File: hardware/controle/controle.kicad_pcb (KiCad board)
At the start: 2 copper layers, 97 x 67.8 mm, 82 parts, among them J1 Barrel_Jack, J10 Conn_01x05_Pin, J11 PWM, J12 ADC, J2 Serial, J3 PWR, J4 DATA, J5 UART7, J6 TWI3, J7 SENS0375, J8 TWI4, J9 LED, Q1 DMG2307L, Q2 DMG2307L, Q3 BSS123, Q4 BSS123, U1 MCP2003B, U2 MCP7940N-xSN, U3 TPS54228, U4 ULN2003, U5 PIC18F05Q40, Y1 32.768Khz

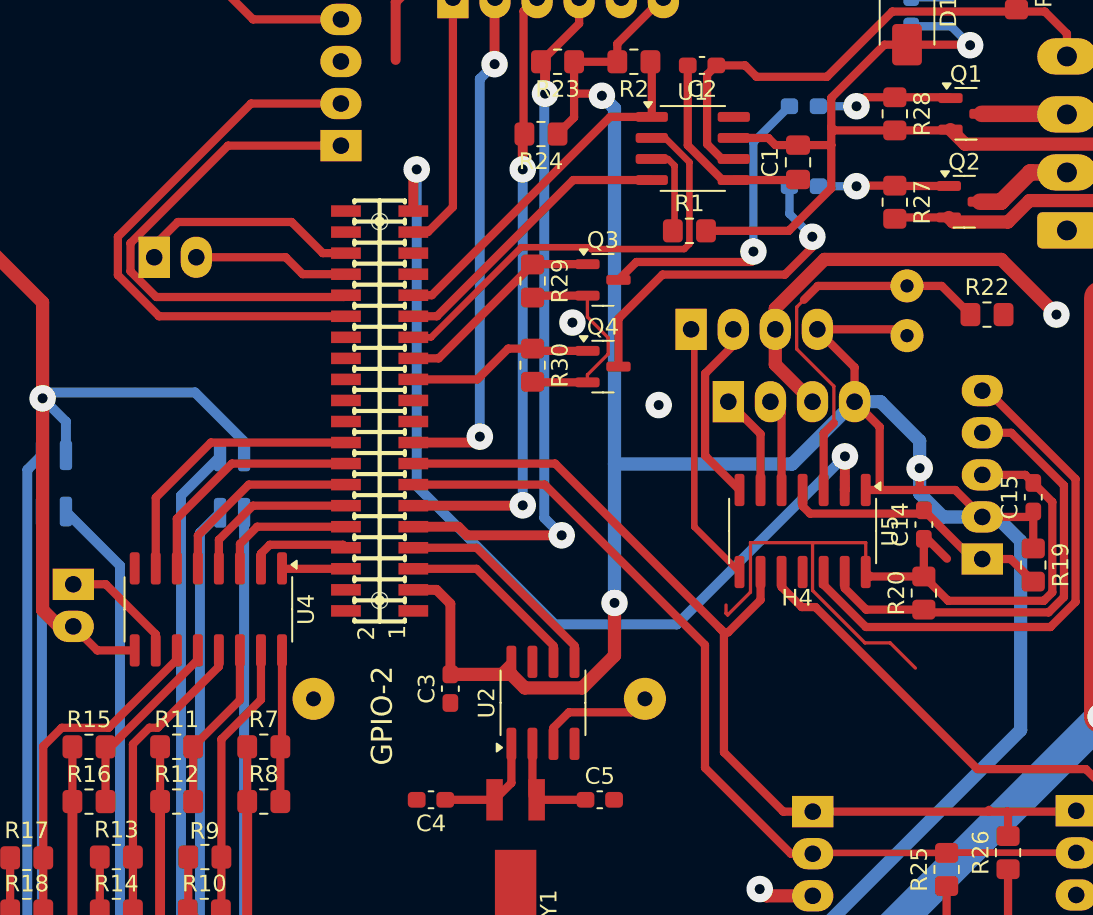
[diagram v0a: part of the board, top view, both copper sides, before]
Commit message: controle: update for DRC
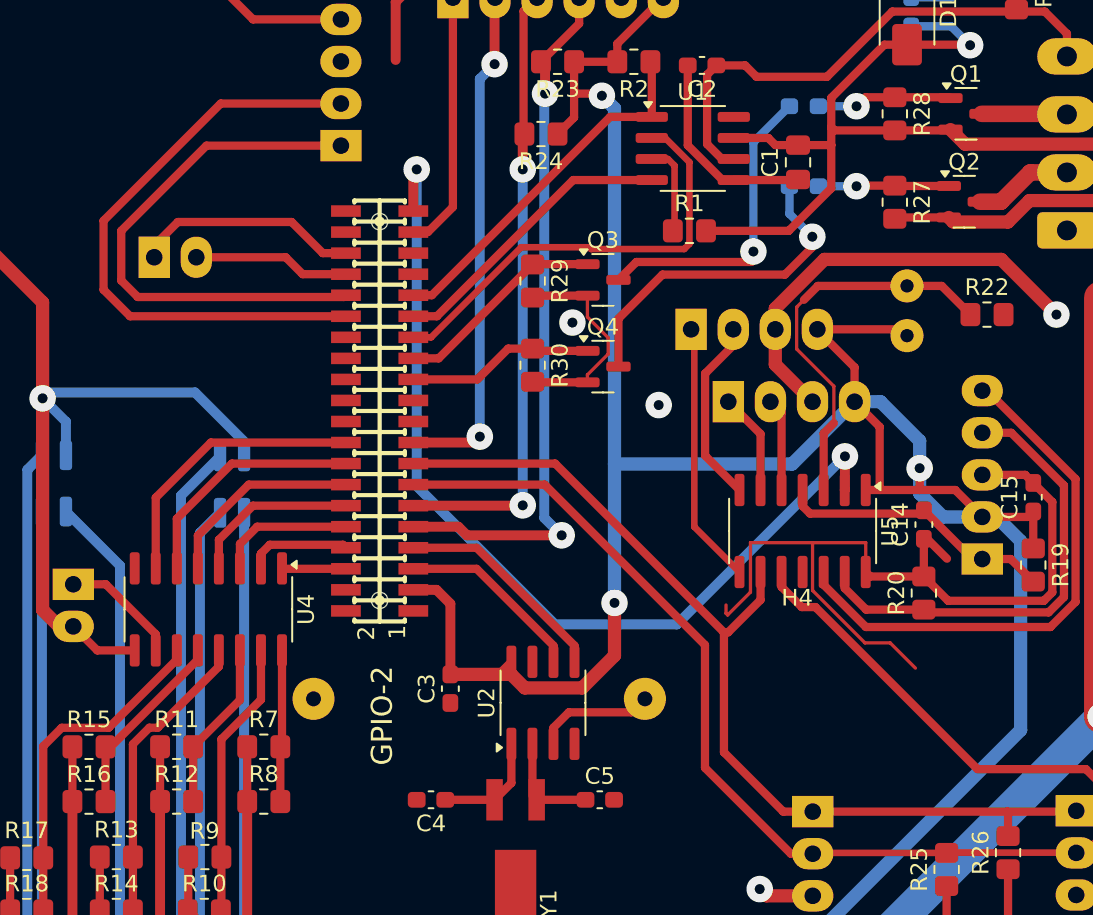
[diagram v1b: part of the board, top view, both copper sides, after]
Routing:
- net /PI21: track 33.9 -> 36.7 mm
- net /PI20: track 30.5 -> 32.4 mm
- net /PI18/UART2_TX: track 13.6 -> 12.9 mm
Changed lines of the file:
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@@
 	)
 	(segment
-		(start 72.0444 77.3076)
+		(start 64.745 90.145)
+		(end 63.1444 88.5444)
+		(width 0.5)
+		(layer "F.Cu")
+		(net 34)
+	)
+	(segment
+		(start 77.773 90.145)
+		(end 64.745 90.145)
+		(width 0.5)
+		(layer "F.Cu")
+		(net 34)
+	)
+	(segment
+		(start 70.2156 77.3076)
 		(end 77.47 77.3076)
 		(width 0.5)
@@
 	)
 	(segment
-		(start 64.008 85.344)
-		(end 72.0444 77.3076)
+		(start 63.1444 88.5444)
+		(end 63.1444 84.3788)
 		(width 0.5)
 		(layer "F.Cu")
@@
 	)
 	(segment
-		(start 77.773 90.145)
-		(end 66.493151 90.145)
-		(width 0.5)
-		(layer "F.Cu")
-		(net 34)
-	)
-	(segment
-		(start 64.008 87.659849)
-		(end 64.008 85.344)
-		(width 0.5)
-		(layer "F.Cu")
-		(net 34)
-	)
-	(segment
-		(start 66.493151 90.145)
-		(end 64.008 87.659849)
+		(start 63.1444 84.3788)
+		(end 70.2156 77.3076)
 		(width 0.5)
 		(layer "F.Cu")
@@
 	)
 	(segment
-		(start 70.655301 79.8476)
-		(end 77.47 79.8476)
-		(width 0.5)
-		(layer "F.Cu")
-		(net 46)
-	)
-	(segment
-		(start 64.77 85.732901)
-		(end 70.655301 79.8476)
-		(width 0.5)
-		(layer "F.Cu")
-		(net 46)
-	)
-	(segment
-		(start 64.77 87.431899)
-		(end 64.77 85.732901)
+		(start 65.208 88.9824)
+		(end 64.2112 87.9856)
 		(width 0.5)
 		(layer "F.Cu")
@@
 	)
 	(segment
-		(start 66.320501 88.9824)
-		(end 64.77 87.431899)
+		(start 64.2112 87.9856)
+		(end 64.2112 84.9884)
 		(width 0.5)
 		(layer "F.Cu")
@@
 	)
 	(segment
+		(start 69.352 79.8476)
+		(end 77.47 79.8476)
+		(width 0.5)
+		(layer "F.Cu")
+		(net 46)
+	)
+	(segment
+		(start 64.2112 84.9884)
+		(end 69.352 79.8476)
+		(width 0.5)
+		(layer "F.Cu")
+		(net 46)
+	)
+	(segment
 		(start 77.6656 88.9824)
-		(end 66.320501 88.9824)
+		(end 65.208 88.9824)
 		(width 0.5)
 		(layer "F.Cu")
@@
 	)
 	(segment
-		(start 66.2004 85.883)
-		(end 66.2004 86.5824)
-		(width 0.5)
-		(layer "F.Cu")
-		(net 54)
-	)
-	(segment
 		(start 76.37384 86.335)
 		(end 74.49384 84.455)
@@
 	)
 	(segment
-		(start 100.584 109.22)
-		(end 90.399 99.035)
+		(start 90.399 99.035)
+		(end 100.584 109.22)
 		(width 0.5)
 		(layer "F.Cu")
@@
 	)
 	(segment
-		(start 116.586 120.0404)
-		(end 116.586 119.929684)
-		(width 0.5)
-		(layer "F.Cu")
-		(net 56)
-	)
-	(segment
 		(start 102.7924 107.2656)
 		(end 100.838 109.22)
@@
 		(width 0.5)
 		(layer "F.Cu")
-		(net 56)
-	)
-	(segment
-		(start 100.33 108.966)
-		(end 100.584 109.22)
-		(width 0.5)
-		(layer "F.Cu")

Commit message: hardware/controle: adjust RGB leds resistors
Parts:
- R10, R16: value 330 -> 1k
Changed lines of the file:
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@@
 		(sheetname "LIN")
 		(sheetfile "lin.kicad_sch")
-		(attr smd)
+		(attr smd dnp)
 		(fp_line
 			(start -3.51 1.65)
@@
 			)
 		)
-		(property "Value" "330"
+		(property "Value" "1k"
 			(at 0 1.65 0)
 			(layer "F.Fab")
@@
 			)
 		)
-		(property "Value" "330"
+		(property "Value" "1k"
 			(at 0 1.65 0)
 			(layer "F.Fab")

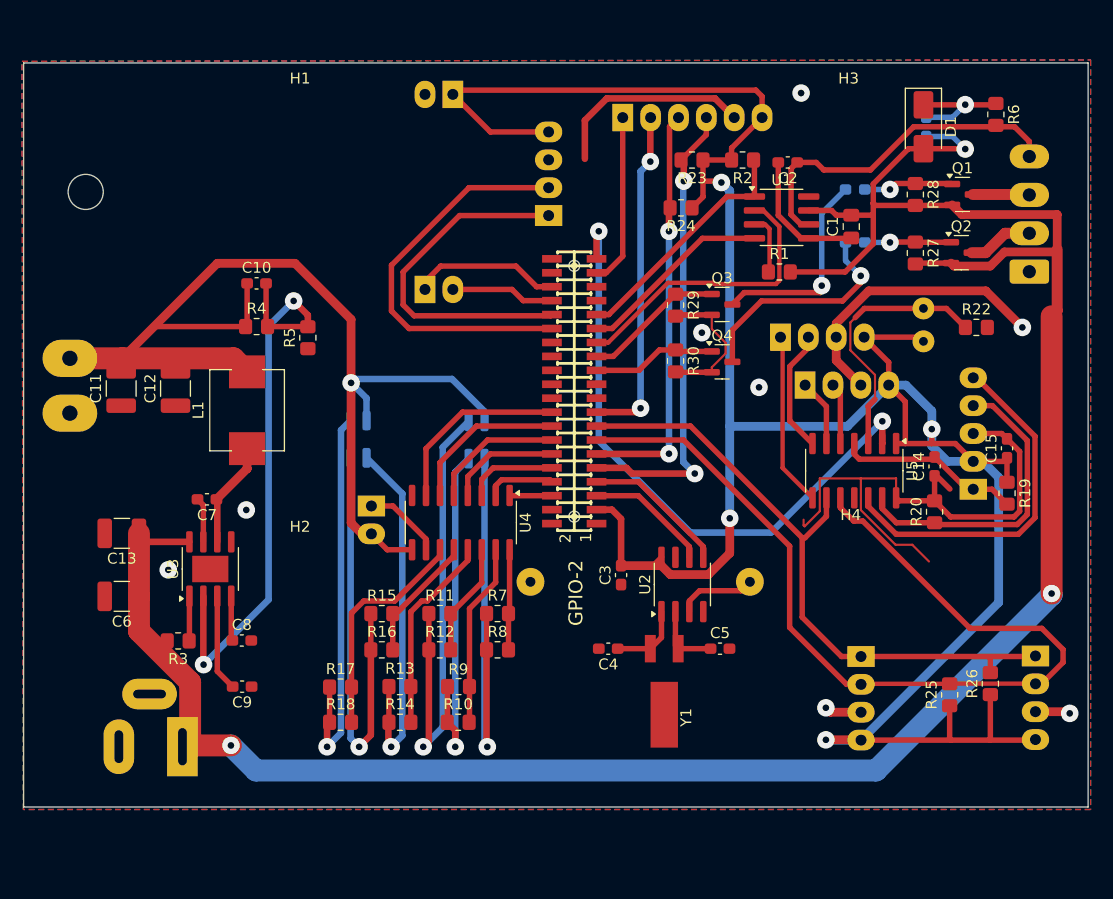
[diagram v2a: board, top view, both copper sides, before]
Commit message: hardware/controle: add fiducials (for OpenPnP)
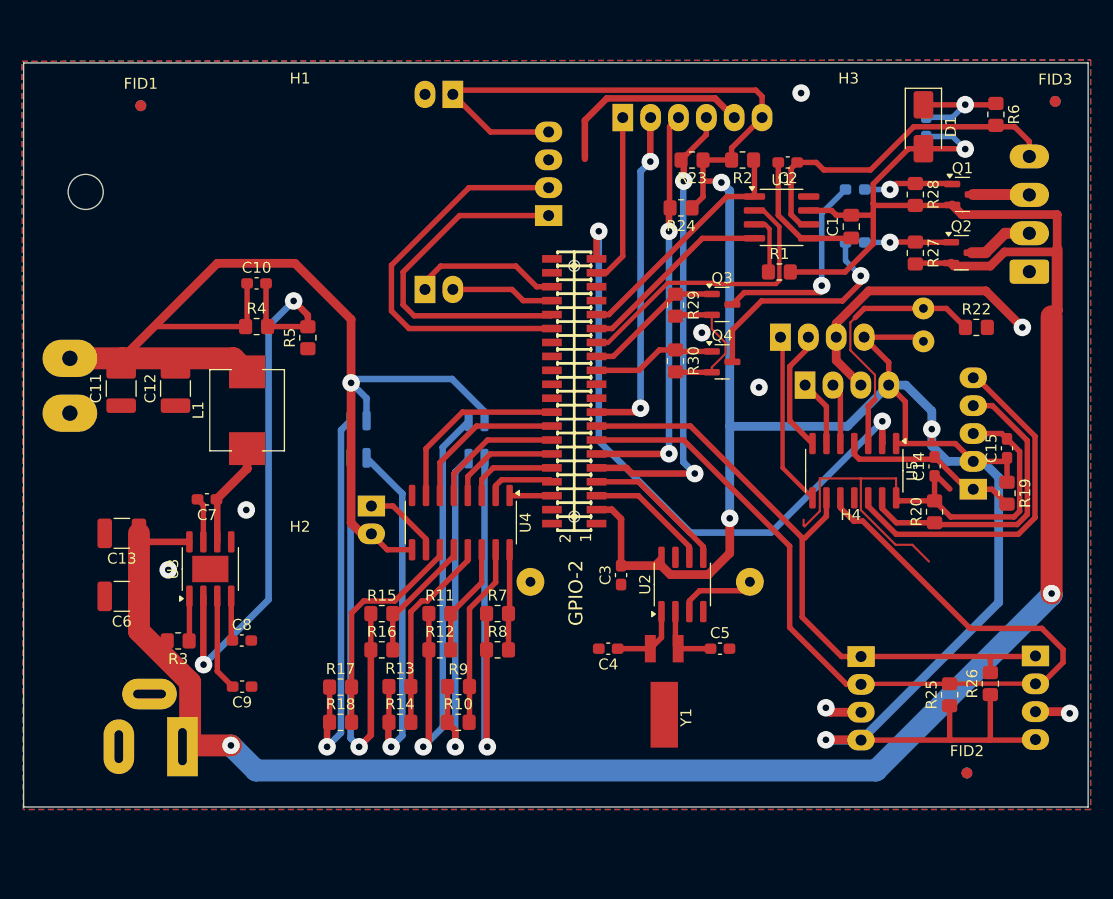
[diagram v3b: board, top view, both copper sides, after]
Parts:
- added FID1: Fiducial, Fiducial:Fiducial_1mm_Mask2mm, F.Cu at (40.3, 69.8)
- added FID2: Fiducial, Fiducial:Fiducial_1mm_Mask2mm, F.Cu at (115.6, 130.7)
- added FID3: Fiducial, Fiducial:Fiducial_1mm_Mask2mm, F.Cu at (123.6, 69.4)
- added FID4: Fiducial, Fiducial:Fiducial_1mm_Mask2mm, B.Cu at (40.3, 69.8)
- added FID5: Fiducial, Fiducial:Fiducial_1mm_Mask2mm, B.Cu at (115.6, 130.7)
- added FID6: Fiducial, Fiducial:Fiducial_1mm_Mask2mm, B.Cu at (123.6, 69.4)

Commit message: hardware/controle: re-route so that most connectors are on left and right sides, same as the lime2 board
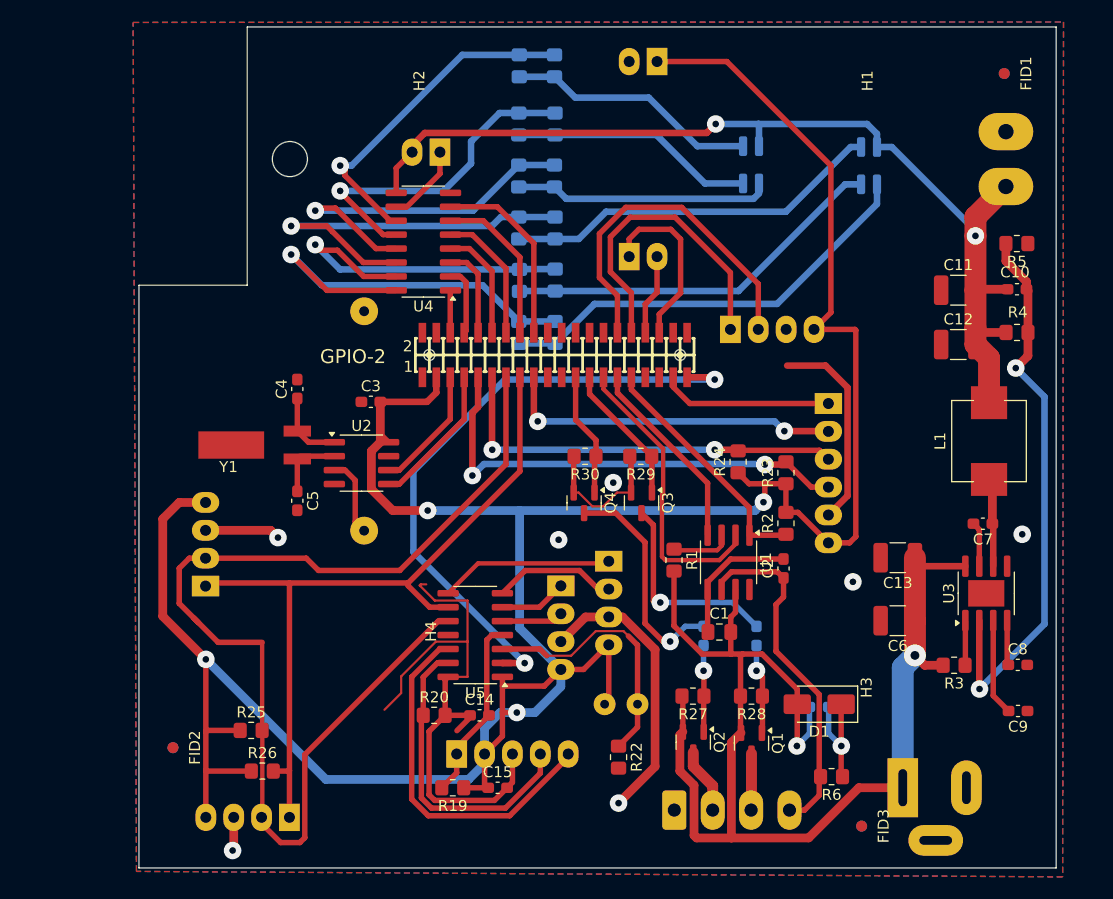
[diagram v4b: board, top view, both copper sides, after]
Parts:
- R10, R11, R12, R13, R14, R15, R16, R17, R18, R7, R8, R9: moved to B.Cu
- moved +5V1 87.8 mm to (119.2, 74.7), turned to -90 degrees
- moved FID1 78.8 mm to (119.0, 66.9), turned to -90 degrees
- moved FID4 78.8 mm to (119.0, 66.9), turned to 90 degrees
- moved C11 76.8 mm to (114.8, 86.7), turned to 0 degrees
- moved J7 75.9 mm to (46.2, 113.6), turned to 0 degrees
- moved FID2 72.4 mm to (43.2, 128.3), turned to -90 degrees
- moved FID5 72.4 mm to (43.2, 128.3), turned to 90 degrees
- moved C12 71.5 mm to (114.8, 91.6), turned to 0 degrees
- moved C13 70.8 mm to (109.3, 111.0)
- moved C6 70.8 mm to (109.3, 116.8)
- moved C8 70.8 mm to (120.2, 120.8)
- moved C7 70.8 mm to (117.1, 107.9)
- moved U3 70.8 mm to (117.4, 114.3)
- moved C9 70.8 mm to (120.3, 125.0)
- moved R3 70.8 mm to (114.4, 120.8)
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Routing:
- net +12V: track 212.8 -> 114.6 mm, vias 3 -> 2
- net +3V3: track 231.1 -> 262.1 mm
- net Net-(U4-O1): track 9.02 -> 37.5 mm, vias 0 -> 1
- net Net-(U4-O3): track 10.3 -> 35.4 mm, vias 0 -> 1
- net Net-(U4-O5): track 10.7 -> 30.0 mm, vias 0 -> 1
- net /PI2/TWI4_SCK: track 84.0 -> 102.3 mm
- net Net-(D3-GK): track 39.2 -> 22.3 mm, vias 1 -> 0
- net Net-(U4-O2): track 16.7 -> 31.4 mm, vias 0 -> 1
- net Net-(U4-O4): track 18.2 -> 32.5 mm, vias 0 -> 1
- net Net-(D3-BK): track 35.8 -> 23.0 mm, vias 1 -> 0
- net /power/+5VCPU: track 103.0 -> 91.7 mm, vias 1 -> 2
- net Net-(U4-O6): track 20.2 -> 30.6 mm, vias 0 -> 1
- net Net-(D3-RK): track 33.7 -> 23.5 mm, vias 1 -> 0
- net /PI3/TWI4_SDA: track 59.1 -> 69.0 mm
- net Net-(D2-BK): track 43.7 -> 34.7 mm, vias 1 -> 0
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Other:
- board size 97 x 67.8 mm -> 83.6 x 76.7 mm

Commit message: hardware/controle: minor PCB adjustements
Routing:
- net GND: track 130.9 -> 131.9 mm
- net +3V3: track 262.1 -> 262.7 mm

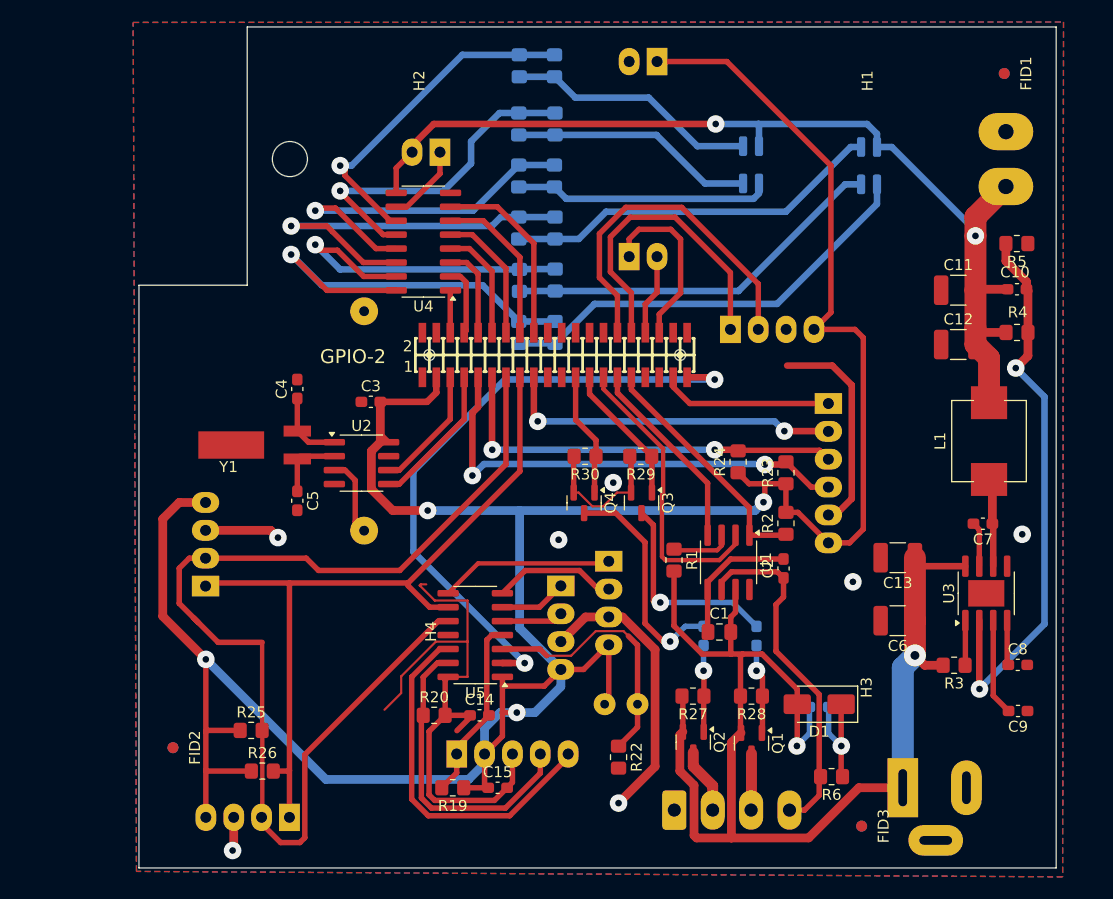
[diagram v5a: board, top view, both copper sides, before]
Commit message: hardware/controle: route control CPU power from pic18
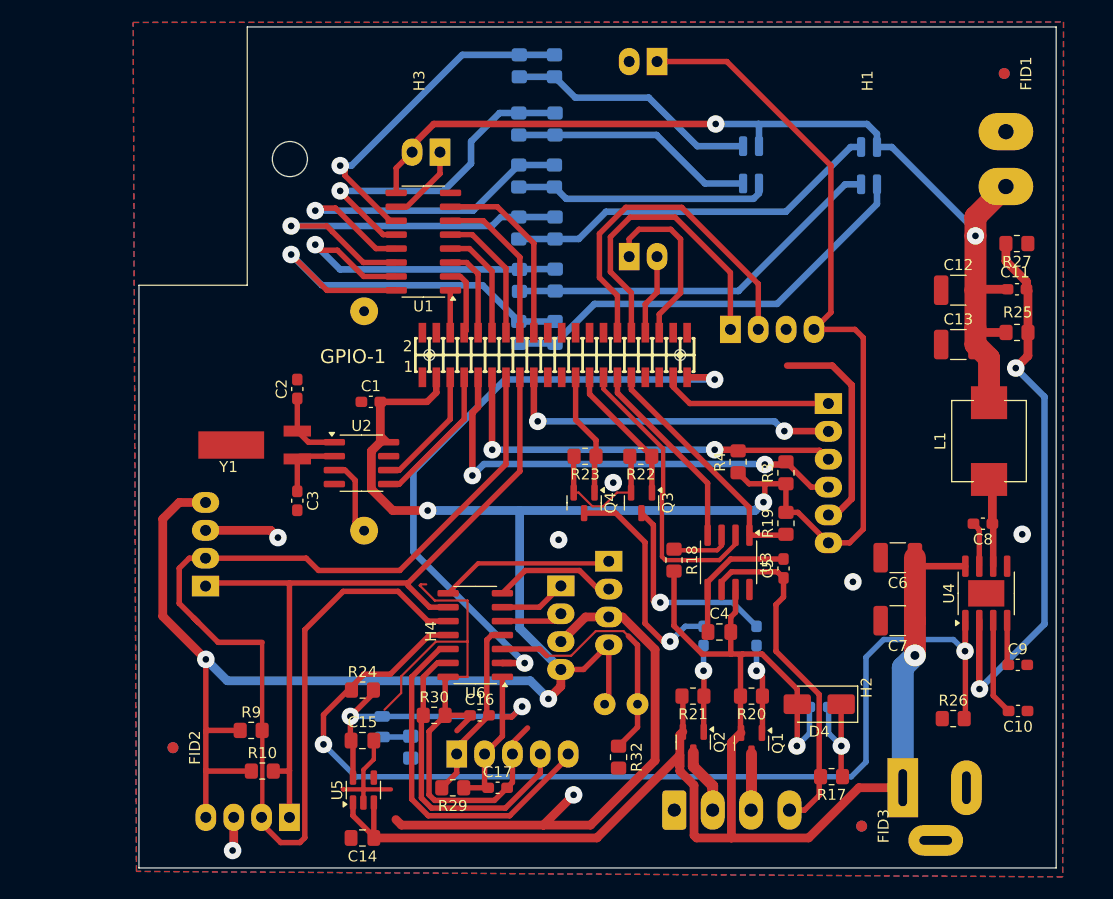
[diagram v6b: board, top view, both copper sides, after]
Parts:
- added C14: 4.7µ, Capacitor_SMD:C_0805_2012Metric_Pad1.18x1.45mm_HandSolder, F.Cu at (60.5, 136.6)
- added C15: 4.7µ, Capacitor_SMD:C_0805_2012Metric_Pad1.18x1.45mm_HandSolder, F.Cu at (60.5, 127.7)
- added D7: Red, LED_SMD:LED_0805_2012Metric, B.Cu at (62.3, 126.4)
- added R26: 56K, Resistor_SMD:R_0805_2012Metric_Pad1.20x1.40mm_HandSolder, F.Cu at (114.3, 125.7)
- added R28: 330, Resistor_SMD:R_0805_2012Metric_Pad1.20x1.40mm_HandSolder, B.Cu at (64.9, 128.3)
- added U5: NCP718xSN330, Package_TO_SOT_SMD:SOT-23-5, F.Cu at (60.6, 132.2)
- R14: renamed from R16; value 1k -> 1K
- R22: renamed from R29; value 47K -> 56K
- R23: renamed from R30; value 47K -> 56K
- R24: renamed from R3; value 10K -> 56K
- R6: renamed from R10; value 1k -> 1K
- moved R24 54.0 mm to (60.5, 123.1), turned to 0 degrees
- renumbered C3 to C1, C9 to C10, C10 to C11, C11 to C12, C12 to C13, C14 to C16, C15 to C17, C4 to C2, C5 to C3, C1 to C4, C2 to C5, C13 to C6, C6 to C7, C7 to C8, C8 to C9, D2 to D1, D3 to D2, D6 to D3, D1 to D4, D4 to D5, D5 to D6, GPIO-2 to GPIO-1, H3 to H2, H2 to H3, H6 to H5, J6 to J1, J12 to J11, J11 to J12, J7 to J2, J8 to J3, J9 to J4, J3 to J6, J4 to J7, J2 to J8, J1 to J9, R7 to R1, R26 to R10, R13 to R11, R14 to R12, R15 to R13, R17 to R15, R18 to R16, R6 to R17, R1 to R18, R2 to R19, R8 to R2, R28 to R20, R27 to R21, R4 to R25, R5 to R27, R19 to R29, R23 to R3, R20 to R30, R21 to R31, R22 to R32, R24 to R4, R9 to R5, R11 to R7, R12 to R8, R25 to R9, U4 to U1, U1 to U3, U3 to U4, U5 to U6
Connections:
- C17 pad 1: +3V3 -> +3.3VP
- J10 pad 2: +3V3 -> +3.3VP
- R24 pad 1: Net-(U3-EN) -> /pic18/VCPU_EN
- R24 pad 2: +12V -> +3.3VP
- R29 pad 1: +3V3 -> +3.3VP
- U4 pad 1: Net-(U3-EN) -> /pic18/VCPU_EN
- U6 pad 1: +3V3 -> +3.3VP
- U6 pad 11: unconnected-(U5-RA2/VREF--Pad11) -> /pic18/VCPU_EN
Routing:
- net /pic18/VCPU_EN: track 0.00 -> 99.8 mm, vias 0 -> 2
- net +3.3VP: track 0.00 -> 40.3 mm, vias 0 -> 2
- net GND: track 131.9 -> 170.3 mm
- net +12V: track 114.6 -> 150.8 mm
- net +3V3: track 262.7 -> 234.3 mm
- net /PI2/TWI4_SCK: track 102.3 -> 111.2 mm
- net Net-(U3-EN): track 4.05 -> 0.00 mm
- net Net-(D7-K): track 0.00 -> 2.63 mm
